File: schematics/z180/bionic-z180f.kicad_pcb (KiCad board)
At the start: 2 copper layers, 25.4 x 68.6 mm, 11 parts, among them J1 Bionic-P135, J2 Bionic-P245, U1 Z80180FSC, U2 11AA010-I/TT, U3 74AHCT157

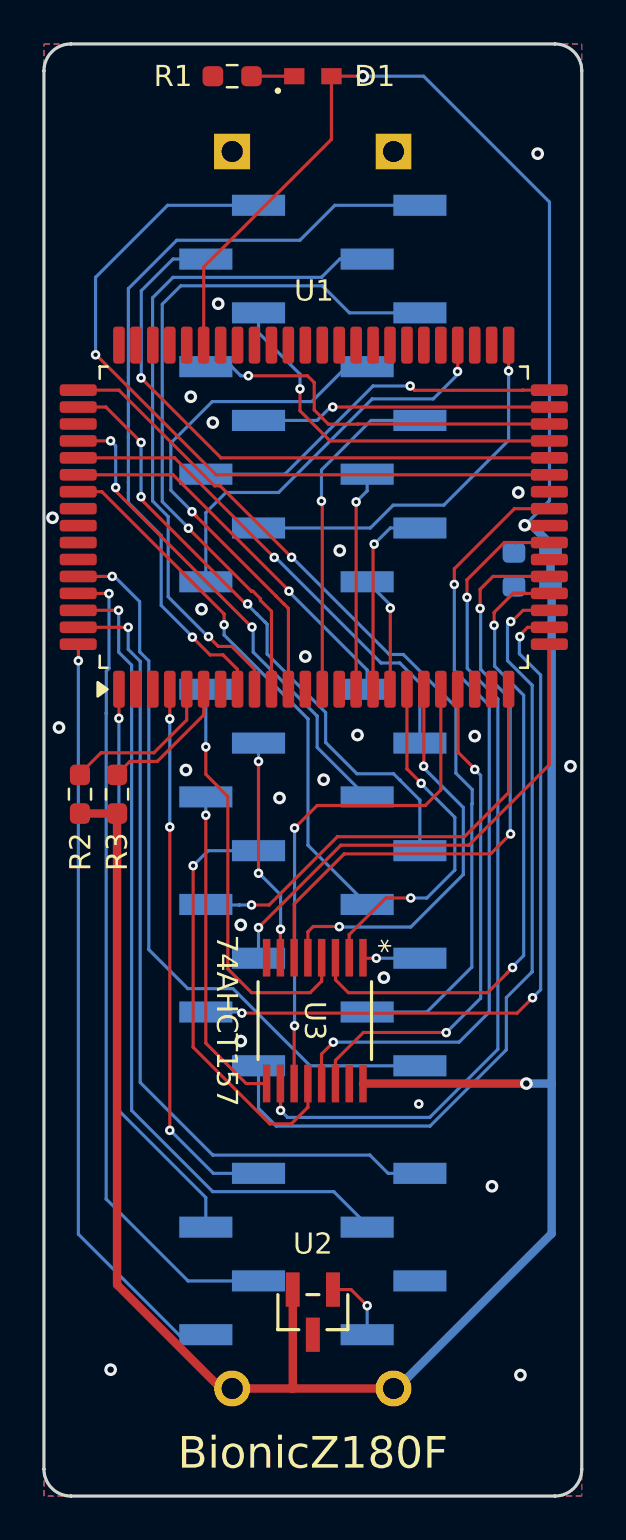
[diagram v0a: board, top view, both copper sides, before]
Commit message: [schematics] Straighten board tracks and regenerate Gerbers
straighten_tracks.py on every routed board: router leftovers snapped to
0/45/90 degrees and redundant segments merged, each pass DRC-checked
(counts unchanged). Gerbers and drill files of the changed boards are
regenerated with each board's plot settings, keeping the committed file
sets; tms9980 keeps its tracks (the rebuild left a dangling VCC stub).
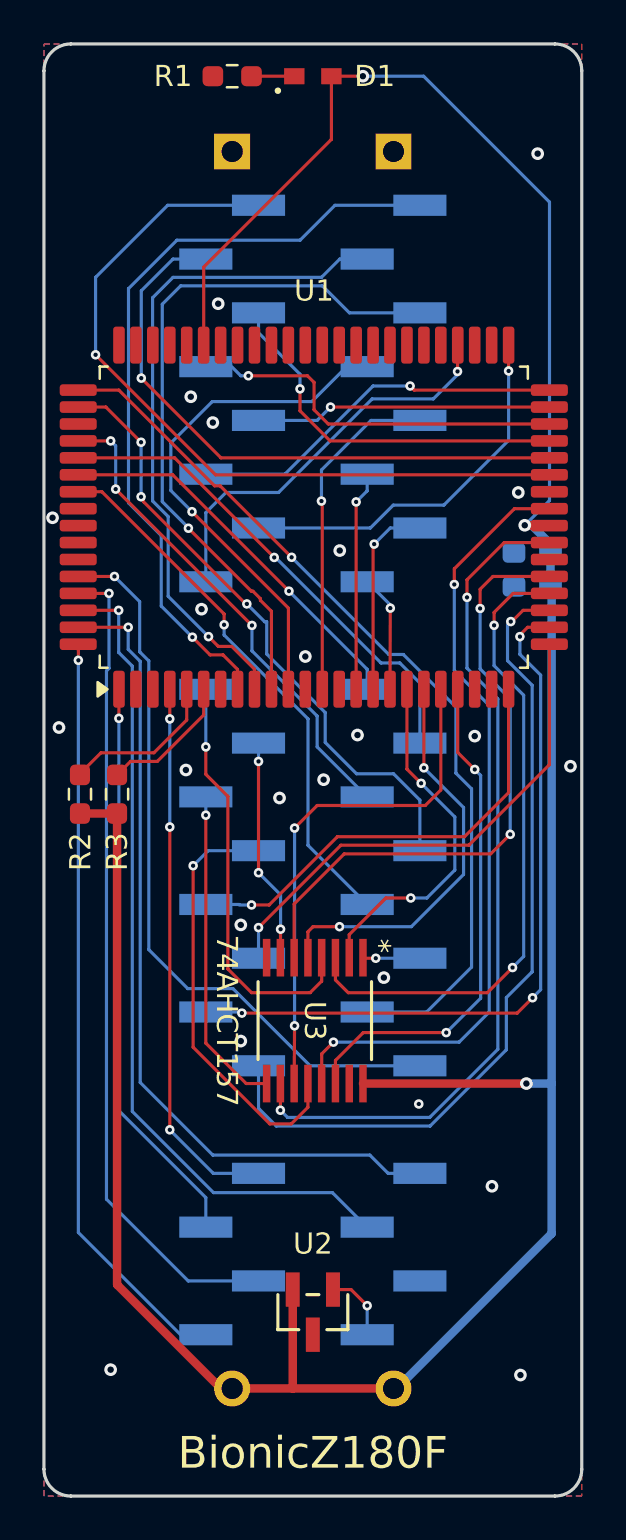
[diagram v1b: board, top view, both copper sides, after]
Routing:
- net ~{RESET}: track 35.9 -> 34.6 mm
- net D3: track 18.1 -> 16.9 mm
- net VCC: track 142.2 -> 141.1 mm
- net A3: track 24.7 -> 23.7 mm

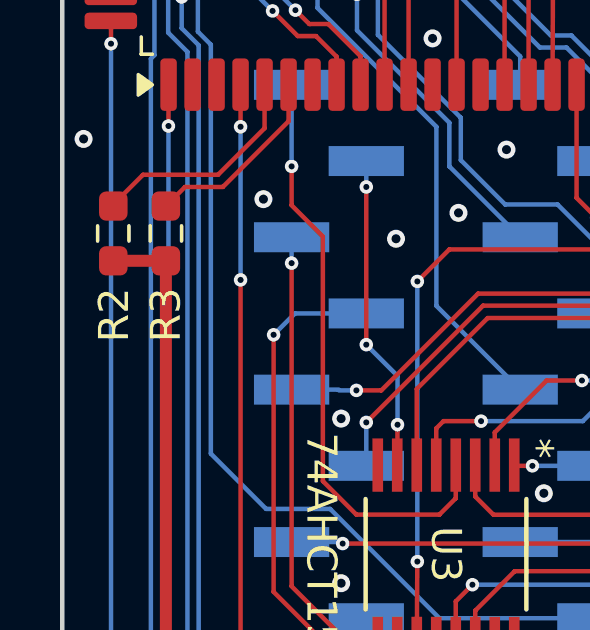
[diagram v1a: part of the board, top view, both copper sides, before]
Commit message: [schematics] Align silkscreen reference labels
align_silk.py snaps each footprint kind's labels onto their common
offset and angle and clears labels DRC flags on silkscreen; 76 labels on
22 boards, no DRC count grows. Their Gerbers are regenerated.
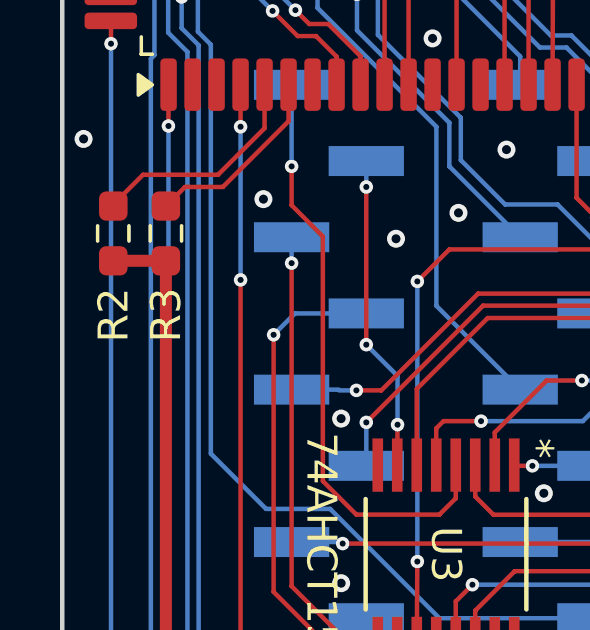
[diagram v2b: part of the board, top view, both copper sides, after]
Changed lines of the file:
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@@
 		(tags "resistor handsolder")
 		(property "Reference" "R3"
-			(at -2.7178 0 90)
+			(at -2.72 0.01 90)
 			(layer "F.SilkS")
 			(effects
@@
 		(tags "resistor handsolder")
 		(property "Reference" "R2"
-			(at -2.7178 0.0254 90)
+			(at -2.72 0.01 90)
 			(layer "F.SilkS")
 			(effects

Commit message: [schematics] Remove the JLC order-number marker from all boards
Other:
- board text removed: "JLCJLCJLCJLC"
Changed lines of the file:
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@@
-		)
-	)
-	(gr_text "JLCJLCJLCJLC"
-		(at 113.7 137.31 0)
-		(layer "B.SilkS")
-		(effects
-			(font
-				(size 0.8 0.8)
-			)
-			(justify bottom mirror)
 		)
 	)
